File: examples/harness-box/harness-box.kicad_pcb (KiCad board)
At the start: 2 copper layers, 18 parts, among them CN1 212528-0400, Q1 DMN3200U-7, U1 5018761840, U2 DG419LEDY-T1-GE4, U3 DG419LEDY-T1-GE4, U4 SMF16A, U5 STPS2H100ZFY

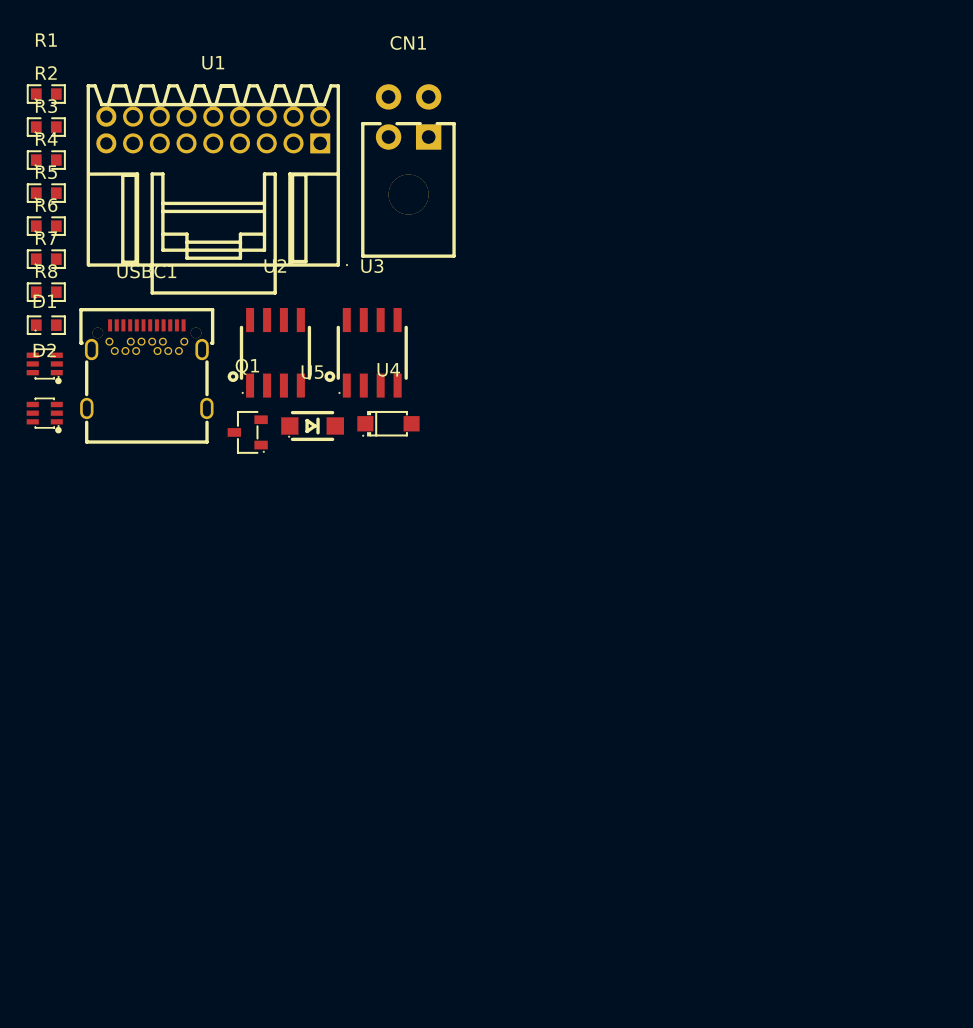
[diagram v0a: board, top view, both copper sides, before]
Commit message: Clean up ts-kicad and complete the harness-box example
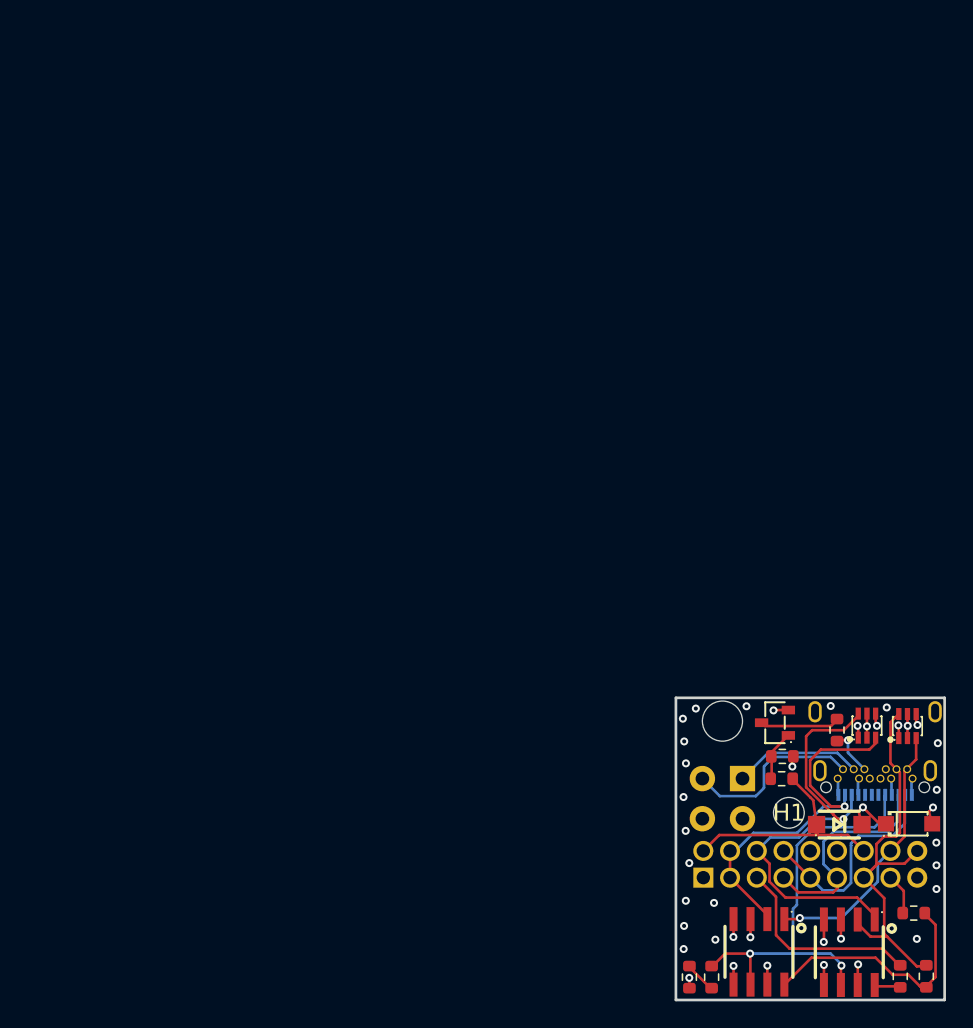
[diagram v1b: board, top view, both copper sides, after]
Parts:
- added H1: MountingHole_2.3mm, , F.Cu at (108.5, 108.6)
- CN1, U1, USBC1: moved to B.Cu
- R1, R2, R3, R4, R5, R6, R7, R8: footprint C21190:R0603 -> Resistor_SMD:R_0603_1608Metric
- moved R1 91.8 mm to (116.8, 120.8), turned to 90 degrees
- moved R2 91.5 mm to (118.7, 120.8), turned to -90 degrees
- moved R3 85.9 mm to (117.8, 116.1)
- moved R4 71.5 mm to (112.0, 102.4), turned to -90 degrees
- moved R7 71.4 mm to (102.7, 120.9), turned to 90 degrees
- moved U1 70.8 mm to (110.0, 112.5), turned to 180 degrees
- moved D1 70.0 mm to (117.3, 102.1), turned to -90 degrees
- moved R5 68.8 mm to (107.9, 106.0)
- moved R8 68.5 mm to (101.0, 120.9), turned to 90 degrees
- moved R6 66.4 mm to (108.0, 104.4), turned to 180 degrees
- moved D2 65.8 mm to (114.3, 102.1), turned to -90 degrees
- moved U2 62.1 mm to (113.0, 119.0), turned to 180 degrees
- moved USBC1 61.7 mm to (114.9, 104.2)
- moved CN1 56.1 mm to (103.5, 107.5)
- moved U3 53.3 mm to (106.2, 119.0), turned to 180 degrees
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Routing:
- net /CAN0_L: track 0.00 -> 33.8 mm, vias 0 -> 1
- net /SBU1: track 0.00 -> 31.7 mm, vias 0 -> 2
- net /CAN2_L: track 0.00 -> 31.5 mm
- net /CAN0_H: track 0.00 -> 28.1 mm, vias 0 -> 1
- net /CAN2_H: track 0.00 -> 20.2 mm, vias 0 -> 1
- net Net-(U3-NO): track 0.00 -> 18.5 mm
- net /IGN_12: track 0.00 -> 18.1 mm
- net /CAN1_L: track 0.00 -> 16.7 mm
- net /CAN1_H: track 0.00 -> 16.3 mm
- net GND: track 0.00 -> 15.9 mm, vias 0 -> 12
- net +12V: track 0.00 -> 15.8 mm, vias 0 -> 7
- net /CAN0_H_TERM: track 0.00 -> 15.7 mm
- net /CAN3_H: track 0.00 -> 13.6 mm
- net /CAN3_L: track 0.00 -> 9.58 mm
- net Net-(Q1-D): track 0.00 -> 5.93 mm
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- added copper zone on In2.Cu, net +12V
- added copper zone on In1.Cu, net GND
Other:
- board outline added: 20.1 x 22.6 mm
- copper layers 2 -> 4
